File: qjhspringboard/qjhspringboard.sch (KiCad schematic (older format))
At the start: 20 parts, among them U1 NE5532

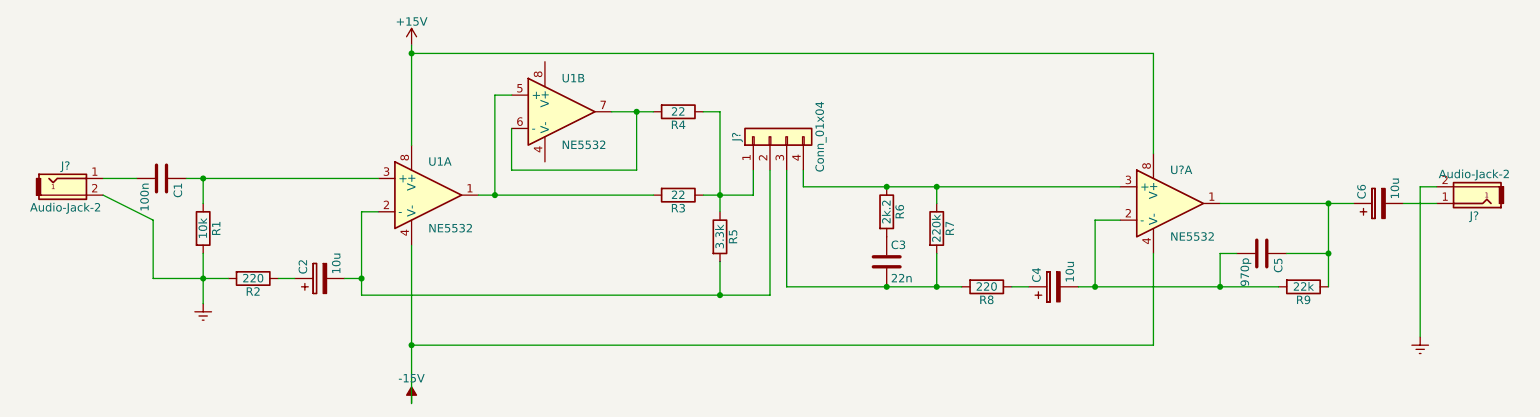
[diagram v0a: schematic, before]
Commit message: schematic is finished other than power connections, pcb layout started and some wiring done, needs power connectors for 15+/-
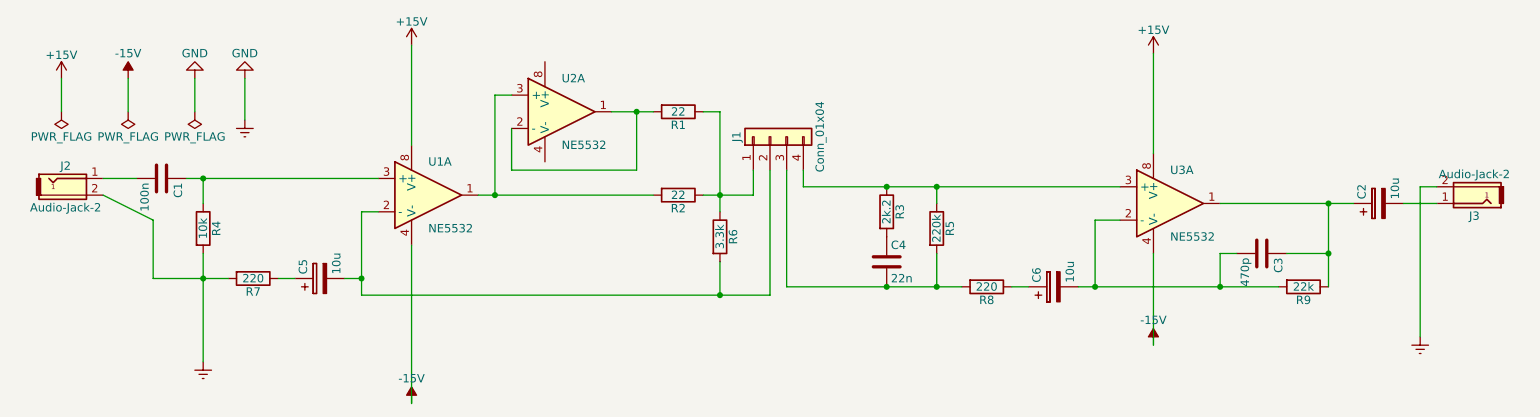
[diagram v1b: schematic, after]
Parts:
- C1: footprint (none) -> Capacitors_THT:C_Disc_D3.8mm_W2.6mm_P2.50mm
- C2: renamed from C6; footprint (none) -> Capacitors_THT:CP_Radial_D5.0mm_P2.50mm
- C3: renamed from C5; value 970p -> 470p; footprint (none) -> Capacitors_SMD:C_0603_HandSoldering
- C4: renamed from C3; footprint (none) -> Capacitors_THT:C_Disc_D3.8mm_W2.6mm_P2.50mm
- C5: renamed from C2; footprint (none) -> Capacitors_THT:CP_Radial_D5.0mm_P2.50mm
- C6: renamed from C4; footprint (none) -> Capacitors_THT:CP_Radial_D5.0mm_P2.50mm
- J1: renamed from J?; footprint (none) -> Pin_Headers:Pin_Header_Straight_1x04_Pitch2.00mm
- J2, J3: renamed from J?; footprint (none) -> Pin_Headers:Pin_Header_Straight_1x02_Pitch2.00mm
- R1: renamed from R4; footprint (none) -> Resistors_THT:R_Axial_DIN0204_L3.6mm_D1.6mm_P7.62mm_Horizontal
- R2: renamed from R3; footprint (none) -> Resistors_THT:R_Axial_DIN0204_L3.6mm_D1.6mm_P7.62mm_Horizontal
- R3: renamed from R6; footprint (none) -> Resistors_THT:R_Axial_DIN0204_L3.6mm_D1.6mm_P7.62mm_Horizontal
- R4: renamed from R1; footprint (none) -> Resistors_THT:R_Axial_DIN0204_L3.6mm_D1.6mm_P7.62mm_Horizontal
- R5: renamed from R7; footprint (none) -> Resistors_THT:R_Axial_DIN0204_L3.6mm_D1.6mm_P7.62mm_Horizontal
- R6: renamed from R5; footprint (none) -> Resistors_THT:R_Axial_DIN0204_L3.6mm_D1.6mm_P7.62mm_Horizontal
- R7: renamed from R2; footprint (none) -> Resistors_THT:R_Axial_DIN0204_L3.6mm_D1.6mm_P7.62mm_Horizontal
- R8, R9: footprint (none) -> Resistors_THT:R_Axial_DIN0204_L3.6mm_D1.6mm_P7.62mm_Horizontal
- U1: footprint (none) -> SMD_Packages:SOIC-8-N
- U2: renamed from U1; footprint (none) -> SMD_Packages:SOIC-8-N
- U3: renamed from U?; footprint (none) -> SMD_Packages:SOIC-8-N
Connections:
- net at R2.2, U1.1: now also U2.3 (+); no longer U2.5 (+)
- new net: R1.2, U2.1, U2.2 (-)
